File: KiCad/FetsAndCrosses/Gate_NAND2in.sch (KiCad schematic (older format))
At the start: 4 parts, among them Q34 BSS84, Q35 2N7002, Q36 2N7002, Q37 BSS84

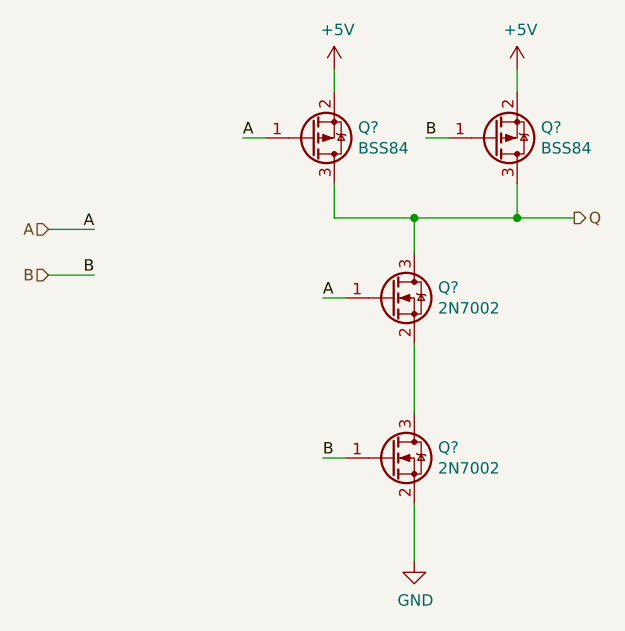
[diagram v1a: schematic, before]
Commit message: Schematic Done, Footprints assigned, ERC OK.
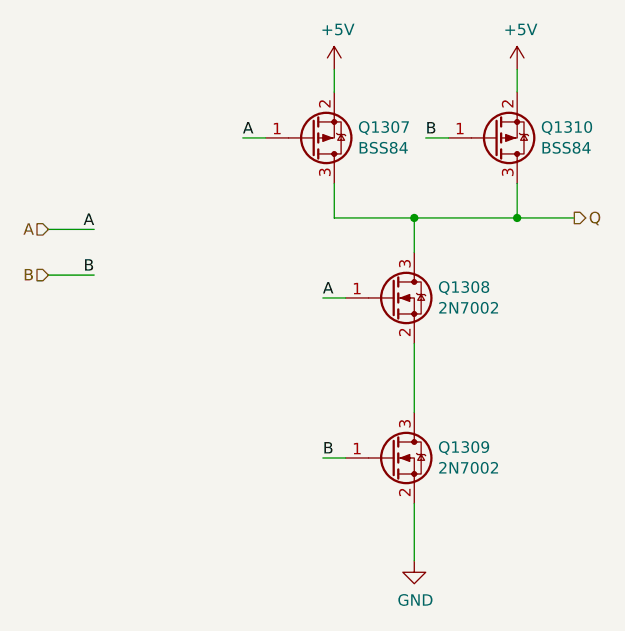
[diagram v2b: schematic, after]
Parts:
- Q771: renamed from Q34; footprint (none) -> LogicQ:SOT-23-P
- Q772: renamed from Q35; footprint (none) -> LogicQ:SOT-23-N
- Q773: renamed from Q36; footprint (none) -> LogicQ:SOT-23-N
- Q774: renamed from Q37; footprint (none) -> LogicQ:SOT-23-P

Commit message: Schematic fixes.
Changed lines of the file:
@@
 $Descr A4 11693 8268
 encoding utf-8
-Sheet 56 389
+Sheet 253 389
 Title ""
-Date ""
-Rev ""
-Comp ""
-Comment1 ""
+Date "2020-07-05"
+Rev "v0.0"
+Comp "Philipp Schilk"
+Comment1 "c"
 Comment2 ""
 Comment3 ""
@@
 AR Path="/5E553405/5F244B15/5E5563DD" Ref="Q707"  Part="1"
 AR Path="/5E553405/5F244B1B/5E5563DD" Ref="Q711"  Part="1"
-F 0 "Q1307" H 6454 2904 50  0000 L CNN
+F 0 "Q897" H 6454 2904 50  0000 L CNN
 F 1 "BSS84" H 6454 2995 50  0000 L CNN
 F 2 "LogicQ:SOT-23-P" H 6450 3050 50  0001 C CNN
@@
 AR Path="/5E553405/5F244B15/5E5563E3" Ref="Q708"  Part="1"
 AR Path="/5E553405/5F244B1B/5E5563E3" Ref="Q712"  Part="1"
-F 0 "Q1308" H 6804 3696 50  0000 L CNN
+F 0 "Q898" H 6804 3696 50  0000 L CNN
 F 1 "2N7002" H 6804 3605 50  0000 L CNN
 F 2 "LogicQ:SOT-23-N" H 6800 3750 50  0001 C CNN
@@
 AR Path="/5E553405/5F244B15/5E55749B" Ref="Q710"  Part="1"
 AR Path="/5E553405/5F244B1B/5E55749B" Ref="Q714"  Part="1"
-F 0 "Q1310" H 7254 2904 50  0000 L CNN
+F 0 "Q900" H 7254 2904 50  0000 L CNN
 F 1 "BSS84" H 7254 2995 50  0000 L CNN
 F 2 "LogicQ:SOT-23-P" H 7250 3050 50  0001 C CNN
@@
 AR Path="/5E553405/5F244B15/5E5584F8" Ref="Q709"  Part="1"
 AR Path="/5E553405/5F244B1B/5E5584F8" Ref="Q713"  Part="1"
-F 0 "Q1309" H 6804 4396 50  0000 L CNN
+F 0 "Q899" H 6804 4396 50  0000 L CNN
 F 1 "2N7002" H 6804 4305 50  0000 L CNN
 F 2 "LogicQ:SOT-23-N" H 6800 4450 50  0001 C CNN

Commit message: Generated Production Files (v0.1)
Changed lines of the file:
@@
 $Descr A4 11693 8268
 encoding utf-8
-Sheet 253 360
+Sheet 61 360
 Title ""
 Date "2020-07-05"
@@
 AR Path="/5FB775FE/5F1827C2/5F46F779/5E5563DD" Ref="Q1366"  Part="1"
 AR Path="/5FB775FE/5F1827D4/5F46F779/5E5563DD" Ref="Q1374"  Part="1"
-F 0 "Q1374" H 6454 2904 50  0000 L CNN
+F 0 "Q243" H 6454 2904 50  0000 L CNN
 F 1 "BSS84" H 6454 2995 50  0000 L CNN
 F 2 "LogicQ:SOT-23-P" H 6450 3050 50  0001 C CNN
@@
 AR Path="/5FB775FE/5F1827C2/5F46F779/5E5563E3" Ref="Q1367"  Part="1"
 AR Path="/5FB775FE/5F1827D4/5F46F779/5E5563E3" Ref="Q1375"  Part="1"
-F 0 "Q1375" H 6804 3696 50  0000 L CNN
+F 0 "Q244" H 6804 3696 50  0000 L CNN
 F 1 "2N7002" H 6804 3605 50  0000 L CNN
 F 2 "LogicQ:SOT-23-N" H 6800 3750 50  0001 C CNN
@@
 AR Path="/5FB775FE/5F1827C2/5F46F779/5E55749B" Ref="Q1369"  Part="1"
 AR Path="/5FB775FE/5F1827D4/5F46F779/5E55749B" Ref="Q1377"  Part="1"
-F 0 "Q1377" H 7254 2904 50  0000 L CNN
+F 0 "Q246" H 7254 2904 50  0000 L CNN
 F 1 "BSS84" H 7254 2995 50  0000 L CNN
 F 2 "LogicQ:SOT-23-P" H 7250 3050 50  0001 C CNN
@@
 AR Path="/5FB775FE/5F1827C2/5F46F779/5E5584F8" Ref="Q1368"  Part="1"
 AR Path="/5FB775FE/5F1827D4/5F46F779/5E5584F8" Ref="Q1376"  Part="1"
-F 0 "Q1376" H 6804 4396 50  0000 L CNN
+F 0 "Q245" H 6804 4396 50  0000 L CNN
 F 1 "2N7002" H 6804 4305 50  0000 L CNN
 F 2 "LogicQ:SOT-23-N" H 6800 4450 50  0001 C CNN
@@
 AR Path="/5FB775FE/5F1827C2/5F46F779/5E5597E5" Ref="#PWR01138"  Part="1"
 AR Path="/5FB775FE/5F1827D4/5F46F779/5E5597E5" Ref="#PWR01144"  Part="1"
-F 0 "#PWR01144" H 6700 4550 50  0001 C CNN
+F 0 "#PWR0261" H 6700 4550 50  0001 C CNN
 F 1 "GND" H 6705 4627 50  0000 C CNN
 F 2 "" H 6700 4800 50  0001 C CNN
@@
 AR Path="/5FB775FE/5F1827C2/5F46F779/5E559D60" Ref="#PWR01139"  Part="1"
 AR Path="/5FB775FE/5F1827D4/5F46F779/5E559D60" Ref="#PWR01145"  Part="1"
-F 0 "#PWR01145" H 6350 2500 50  0001 C CNN
+F 0 "#PWR0262" H 6350 2500 50  0001 C CNN
 F 1 "+5V" H 6365 2823 50  0000 C CNN
 F 2 "" H 6350 2650 50  0001 C CNN
@@
 AR Path="/5FB775FE/5F1827C2/5F46F779/5E55A6E2" Ref="#PWR01140"  Part="1"
 AR Path="/5FB775FE/5F1827D4/5F46F779/5E55A6E2" Ref="#PWR01146"  Part="1"
-F 0 "#PWR01146" H 7150 2500 50  0001 C CNN
+F 0 "#PWR0263" H 7150 2500 50  0001 C CNN
 F 1 "+5V" H 7165 2823 50  0000 C CNN
 F 2 "" H 7150 2650 50  0001 C CNN

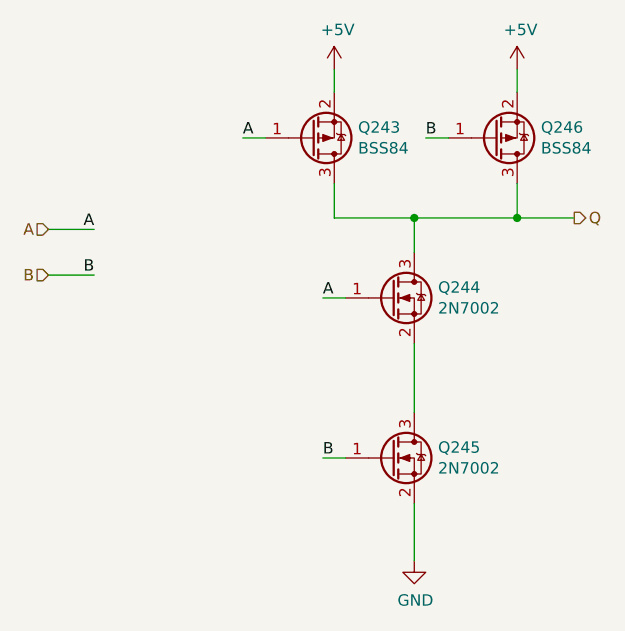
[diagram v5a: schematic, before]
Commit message: Updated Schematic
 - Fixed Mem cell
 - Fixed Draw LED to not light if last move wins game
 - Changed capacitor
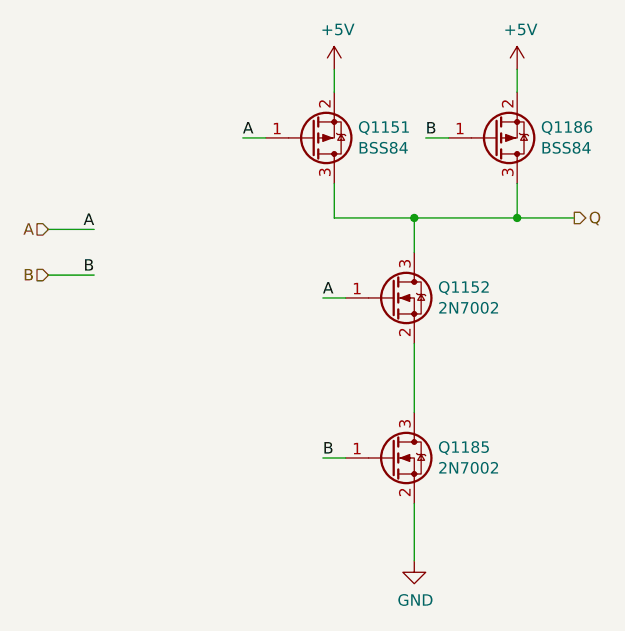
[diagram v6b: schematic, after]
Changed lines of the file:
@@
 $Descr A4 11693 8268
 encoding utf-8
-Sheet 61 360
-Title ""
-Date "2020-07-05"
-Rev "v0.0"
+Sheet 284 362
+Title "Fets and Crosses"
+Date "2020-09-15"
+Rev "v0.2"
 Comp "Philipp Schilk"
-Comment1 "c"
+Comment1 "Tic-Tac-Toe implementation from discrete-transistor CMOS logic"
 Comment2 ""
 Comment3 ""
-Comment4 ""
+Comment4 "https://github.com/TheSchilk/Fets_and_Crosses"
 $EndDescr
 $Comp
@@
 AR Path="/5FB775FE/5F1827C2/5F46F779/5E5563DD" Ref="Q1366"  Part="1"
 AR Path="/5FB775FE/5F1827D4/5F46F779/5E5563DD" Ref="Q1374"  Part="1"
-F 0 "Q243" H 6454 2904 50  0000 L CNN
+F 0 "Q1151" H 6454 2904 50  0000 L CNN
 F 1 "BSS84" H 6454 2995 50  0000 L CNN
 F 2 "LogicQ:SOT-23-P" H 6450 3050 50  0001 C CNN
@@
 AR Path="/5FB775FE/5F1827C2/5F46F779/5E5563E3" Ref="Q1367"  Part="1"
 AR Path="/5FB775FE/5F1827D4/5F46F779/5E5563E3" Ref="Q1375"  Part="1"
-F 0 "Q244" H 6804 3696 50  0000 L CNN
+F 0 "Q1152" H 6804 3696 50  0000 L CNN
 F 1 "2N7002" H 6804 3605 50  0000 L CNN
 F 2 "LogicQ:SOT-23-N" H 6800 3750 50  0001 C CNN
@@
 AR Path="/5FB775FE/5F1827C2/5F46F779/5E55749B" Ref="Q1369"  Part="1"
 AR Path="/5FB775FE/5F1827D4/5F46F779/5E55749B" Ref="Q1377"  Part="1"
-F 0 "Q246" H 7254 2904 50  0000 L CNN
+F 0 "Q1186" H 7254 2904 50  0000 L CNN
 F 1 "BSS84" H 7254 2995 50  0000 L CNN
 F 2 "LogicQ:SOT-23-P" H 7250 3050 50  0001 C CNN
@@
 AR Path="/5FB775FE/5F1827C2/5F46F779/5E5584F8" Ref="Q1368"  Part="1"
 AR Path="/5FB775FE/5F1827D4/5F46F779/5E5584F8" Ref="Q1376"  Part="1"
-F 0 "Q245" H 6804 4396 50  0000 L CNN
+F 0 "Q1185" H 6804 4396 50  0000 L CNN
 F 1 "2N7002" H 6804 4305 50  0000 L CNN
 F 2 "LogicQ:SOT-23-N" H 6800 4450 50  0001 C CNN
@@
 AR Path="/5FB775FE/5F1827C2/5F46F779/5E5597E5" Ref="#PWR01138"  Part="1"
 AR Path="/5FB775FE/5F1827D4/5F46F779/5E5597E5" Ref="#PWR01144"  Part="1"
-F 0 "#PWR0261" H 6700 4550 50  0001 C CNN
+F 0 "#PWR01105" H 6700 4550 50  0001 C CNN
 F 1 "GND" H 6705 4627 50  0000 C CNN
 F 2 "" H 6700 4800 50  0001 C CNN
@@
 AR Path="/5FB775FE/5F1827C2/5F46F779/5E559D60" Ref="#PWR01139"  Part="1"
 AR Path="/5FB775FE/5F1827D4/5F46F779/5E559D60" Ref="#PWR01145"  Part="1"
-F 0 "#PWR0262" H 6350 2500 50  0001 C CNN
+F 0 "#PWR01106" H 6350 2500 50  0001 C CNN
 F 1 "+5V" H 6365 2823 50  0000 C CNN
 F 2 "" H 6350 2650 50  0001 C CNN
@@
 AR Path="/5FB775FE/5F1827C2/5F46F779/5E55A6E2" Ref="#PWR01140"  Part="1"
 AR Path="/5FB775FE/5F1827D4/5F46F779/5E55A6E2" Ref="#PWR01146"  Part="1"
-F 0 "#PWR0263" H 7150 2500 50  0001 C CNN
+F 0 "#PWR01107" H 7150 2500 50  0001 C CNN
 F 1 "+5V" H 7165 2823 50  0000 C CNN
 F 2 "" H 7150 2650 50  0001 C CNN

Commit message: PCB v1.0 layout mostly done.
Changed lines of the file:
@@
 AR Path="/5FB775FE/5F1827C2/5F46F779/5E5563DD" Ref="Q1366"  Part="1"
 AR Path="/5FB775FE/5F1827D4/5F46F779/5E5563DD" Ref="Q1374"  Part="1"
-F 0 "Q1151" H 6454 2904 50  0000 L CNN
+F 0 "Q1374" H 6454 2904 50  0000 L CNN
 F 1 "BSS84" H 6454 2995 50  0000 L CNN
 F 2 "LogicQ:SOT-23-P" H 6450 3050 50  0001 C CNN
@@
 AR Path="/5FB775FE/5F1827C2/5F46F779/5E5563E3" Ref="Q1367"  Part="1"
 AR Path="/5FB775FE/5F1827D4/5F46F779/5E5563E3" Ref="Q1375"  Part="1"
-F 0 "Q1152" H 6804 3696 50  0000 L CNN
+F 0 "Q1375" H 6804 3696 50  0000 L CNN
 F 1 "2N7002" H 6804 3605 50  0000 L CNN
 F 2 "LogicQ:SOT-23-N" H 6800 3750 50  0001 C CNN
@@
 AR Path="/5FB775FE/5F1827C2/5F46F779/5E55749B" Ref="Q1369"  Part="1"
 AR Path="/5FB775FE/5F1827D4/5F46F779/5E55749B" Ref="Q1377"  Part="1"
-F 0 "Q1186" H 7254 2904 50  0000 L CNN
+F 0 "Q1377" H 7254 2904 50  0000 L CNN
 F 1 "BSS84" H 7254 2995 50  0000 L CNN
 F 2 "LogicQ:SOT-23-P" H 7250 3050 50  0001 C CNN
@@
 AR Path="/5FB775FE/5F1827C2/5F46F779/5E5584F8" Ref="Q1368"  Part="1"
 AR Path="/5FB775FE/5F1827D4/5F46F779/5E5584F8" Ref="Q1376"  Part="1"
-F 0 "Q1185" H 6804 4396 50  0000 L CNN
+F 0 "Q1376" H 6804 4396 50  0000 L CNN
 F 1 "2N7002" H 6804 4305 50  0000 L CNN
 F 2 "LogicQ:SOT-23-N" H 6800 4450 50  0001 C CNN
@@
 AR Path="/5FB775FE/5F1827C2/5F46F779/5E5597E5" Ref="#PWR01138"  Part="1"
 AR Path="/5FB775FE/5F1827D4/5F46F779/5E5597E5" Ref="#PWR01144"  Part="1"
-F 0 "#PWR01105" H 6700 4550 50  0001 C CNN
+F 0 "#PWR01144" H 6700 4550 50  0001 C CNN
 F 1 "GND" H 6705 4627 50  0000 C CNN
 F 2 "" H 6700 4800 50  0001 C CNN
@@
 AR Path="/5FB775FE/5F1827C2/5F46F779/5E559D60" Ref="#PWR01139"  Part="1"
 AR Path="/5FB775FE/5F1827D4/5F46F779/5E559D60" Ref="#PWR01145"  Part="1"
-F 0 "#PWR01106" H 6350 2500 50  0001 C CNN
+F 0 "#PWR01145" H 6350 2500 50  0001 C CNN
 F 1 "+5V" H 6365 2823 50  0000 C CNN
 F 2 "" H 6350 2650 50  0001 C CNN
@@
 AR Path="/5FB775FE/5F1827C2/5F46F779/5E55A6E2" Ref="#PWR01140"  Part="1"
 AR Path="/5FB775FE/5F1827D4/5F46F779/5E55A6E2" Ref="#PWR01146"  Part="1"
-F 0 "#PWR01107" H 7150 2500 50  0001 C CNN
+F 0 "#PWR01146" H 7150 2500 50  0001 C CNN
 F 1 "+5V" H 7165 2823 50  0000 C CNN
 F 2 "" H 7150 2650 50  0001 C CNN
